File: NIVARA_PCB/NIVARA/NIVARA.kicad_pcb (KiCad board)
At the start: 4 copper layers, 101.2 x 82 mm, 89 parts, among them J1 Power, J10 I_ANALOG, J11 RS485, J12 O_ANALOG, J3 I_NPN, J4 I_PNP, J5 RELAY_1, J6 RELAY_2, J7 O_NPN, J8 O_PNP, J9 I_DIG, Q1 PMBT3904, Q2 PMBT3904, U1 AP63203WU, U10 GP8201S-TC50-EW, U2 AT3H4A-CUH-S, U3 AT3H4A-CUH-S, U4 AT3H4A-CUH-S, U5 AT3H4A-CUH-S, U6 AT3H4A-CUH-S, U7 TD321D485H-A-LB, U8 AT3H4A-CUH-S, U9 GP8303-TC50-EW

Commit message: Se organizaron componentes en el area de PCB
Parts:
- removed C3: C_0603, PCM_Capacitor_SMD_AKL:C_0603_1608Metric
- removed D1: 1N4007, Diode_SMD:D_SOD-123F
- removed L1: L_Iron, Inductor_SMD:L_0201_0603Metric_Pad0.64x0.40mm_HandSolder
- removed Q1: PMBT3904, PCM_Package_TO_SOT_SMD_AKL:SOT-23
- removed R1, R2, R30: 22K, PCM_Resistor_SMD_AKL:R_0603_1608Metric
- removed R23, R31: ?, PCM_Resistor_SMD_AKL:R_0603_1608Metric
- removed R36: ?, PCM_Resistor_SMD_AKL:R_1206_3216Metric_Pad1.30x1.75mm_HandSolder
- removed RLY1: SRD-24VDC-SL-C, easyeda2kicad:RELAY-TH_SRD-XXVDC-XL-C
- removed TP8: TestPoint, TestPoint:TestPoint_THTPad_D1.0mm_Drill0.5mm
- added C16: 220uF, PCM_Capacitor_SMD_AKL:C_0603_1608Metric, F.Cu at (1.18, -49.9)
- added C17: 1uF, PCM_Capacitor_SMD_AKL:C_0603_1608Metric, F.Cu at (1.18, -47.2)
- added C18: 100nF, PCM_Capacitor_SMD_AKL:C_0603_1608Metric, F.Cu at (1.18, -44.5)
- added C19: 1uF, PCM_Capacitor_SMD_AKL:C_0603_1608Metric, F.Cu at (-21.5, -17.4)
- added C20: 100nF, PCM_Capacitor_SMD_AKL:C_0603_1608Metric, F.Cu at (-21.5, -14.6)
- added C21: 1uF, PCM_Capacitor_SMD_AKL:C_0603_1608Metric, F.Cu at (8.18, -23.5)
- added C22: 100nF, PCM_Capacitor_SMD_AKL:C_0603_1608Metric, F.Cu at (8.18, -20.8)
- added C9: 1uF, PCM_Capacitor_SMD_AKL:C_0603_1608Metric, F.Cu at (1.18, -52.6)
- added D4: 1N4007, Diode_SMD:D_SOD-123F, F.Cu at (14.5, -38.6)
- added D5: SM6T24A, Diode_SMD:D_SMB, F.Cu at (17.4, -26.6)
- added D6: SM6T12A, Diode_SMD:D_SMB, F.Cu at (-19.5, -21.5)
- added D7: SM6T12A, Diode_SMD:D_SMB, F.Cu at (3.22, -27.7)
- added JP2: A0, Jumper:SolderJumper-2_P1.3mm_Open_RoundedPad1.0x1.5mm, F.Cu at (1.17, -41.3)
- added JP3: A1, Jumper:SolderJumper-2_P1.3mm_Open_RoundedPad1.0x1.5mm, F.Cu at (1.17, -37.8)
- added JP4: A2, Jumper:SolderJumper-2_P1.3mm_Open_RoundedPad1.0x1.5mm, F.Cu at (1.17, -34.2)
- added L2: FNR5020S3R9NT, easyeda2kicad:IND-SMD_L5.0-W5.0_FNR50XXS, F.Cu at (72.3, 119.9)
- added Q3: BRCS4435SC, easyeda2kicad:SOP-8_L5.0-W4.0-P1.27-LS6.0-BL, F.Cu at (12.9, -49.7)
- added Q4: PMBT3904, PCM_Package_TO_SOT_SMD_AKL:SOT-23, F.Cu at (75.7, -47.4)
- added R10: 1K, PCM_Resistor_SMD_AKL:R_0603_1608Metric, F.Cu at (6.39, -45.5)
- added R11: 2.5K, PCM_Resistor_SMD_AKL:R_0603_1608Metric, F.Cu at (5.41, -36.9)
- added R12: 100K, PCM_Resistor_SMD_AKL:R_0603_1608Metric, F.Cu at (5.41, -34.1)
- added R13: 15R, PCM_Resistor_SMD_AKL:R_1206_3216Metric, F.Cu at (14.6, -42.0)
- added R14: 0R, PCM_Resistor_SMD_AKL:R_0603_1608Metric, F.Cu at (-17.3, -17.4)
- added R15: 0R, PCM_Resistor_SMD_AKL:R_0603_1608Metric, F.Cu at (9.45, -29.1)
- added R16: ?, PCM_Resistor_SMD_AKL:R_0603_1608Metric, F.Cu at (47.1, 87.8)
- added R17: ?, PCM_Resistor_SMD_AKL:R_0603_1608Metric, F.Cu at (48.5, -36.4)
- added R43: 22K, PCM_Resistor_SMD_AKL:R_0603_1608Metric, F.Cu at (71.3, -48.4)
- added R44: ?, PCM_Resistor_SMD_AKL:R_0603_1608Metric, F.Cu at (71.3, -45.7)
- added R7: 150R, PCM_Resistor_SMD_AKL:R_0603_1608Metric, F.Cu at (161.0, 132.4)
- added R8: 1K, PCM_Resistor_SMD_AKL:R_0603_1608Metric, F.Cu at (6.39, -52.3)
- added R9: 1K, PCM_Resistor_SMD_AKL:R_0603_1608Metric, F.Cu at (6.39, -48.9)
- added RLY3: SRD-24VDC-SL-C, easyeda2kicad:RELAY-TH_SRD-XXVDC-XL-C, F.Cu at (125.5, 79.5)
- added TP12: TestPoint, TestPoint:TestPoint_THTPad_D1.0mm_Drill0.5mm, F.Cu at (46.6, 87.8)
- added U11: ESP32-S3-WROOM-1, PCM_Espressif:ESP32-S3-WROOM-1, F.Cu at (153.5, 119.2)
- added U12: ZMM12V_C5345999, easyeda2kicad:LL-34_L3.5-W1.5-RD-2, F.Cu at (14.6, -34.9)
- added U13: GP8201S-TC50-EW, easyeda2kicad:ESOP-8_L4.9-W3.9-P1.27-LS6.0-BL-EP, F.Cu at (2.82, -20.9)
- added kibuzzard-68857B38: G***, kibuzzard-68857B38, F.Cu at (161.0, 134.4)
- added kibuzzard-688671E8: G***, kibuzzard-688671E8, F.Cu at (81.3, 127.7)
- added kibuzzard-688672FE: G***, kibuzzard-688672FE, F.Cu at (81.3, 128.7)
- added kibuzzard-68867375: G***, kibuzzard-68867375, F.Cu at (81.3, 129.7)
- added kibuzzard-68867375: G***, kibuzzard-68867375, F.Cu at (93.9, 129.8)
- added kibuzzard-68867375: G***, kibuzzard-68867375, F.Cu at (87.4, 129.7)
- added kibuzzard-68867375: G***, kibuzzard-68867375, F.Cu at (100.0, 129.7)
- added kibuzzard-688673E6: G***, kibuzzard-688673E6, F.Cu at (87.4, 127.7)
- added kibuzzard-6886740D: G***, kibuzzard-6886740D, F.Cu at (87.4, 128.7)
- added kibuzzard-68868B65: G***, kibuzzard-68868B65, F.Cu at (161.0, 135.9)
- added kibuzzard-68868CAC: G***, kibuzzard-68868CAC, F.Cu at (71.1, 133.0)
- added kibuzzard-68868CE5: G***, kibuzzard-68868CE5, F.Cu at (76.2, 133.0)
- added kibuzzard-68868D86: G***, kibuzzard-68868D86, F.Cu at (83.7, 133.0)
- added kibuzzard-68868DBB: G***, kibuzzard-68868DBB, F.Cu at (88.8, 133.0)
- added kibuzzard-68868E7D: G***, kibuzzard-68868E7D, F.Cu at (96.3, 133.0)
- added kibuzzard-68868E8A: G***, kibuzzard-68868E8A, F.Cu at (101.4, 133.0)
- added kibuzzard-68868F64: G***, kibuzzard-68868F64, F.Cu at (108.6, 133.0)
- added kibuzzard-68868F72: G***, kibuzzard-68868F72, F.Cu at (113.7, 133.0)
- added kibuzzard-68869F01: G***, kibuzzard-68869F01, F.Cu at (87.4, 130.7)
- added kibuzzard-68869F01: G***, kibuzzard-68869F01, F.Cu at (81.3, 130.7)
- added kibuzzard-6886A071: G***, kibuzzard-6886A071, F.Cu at (99.5, 116.1)
- added kibuzzard-6886A071: G***, kibuzzard-6886A071, F.Cu at (93.4, 116.2)
- added kibuzzard-6886A0F4: G***, kibuzzard-6886A0F4, F.Cu at (80.8, 114.6)
- added kibuzzard-6886A148: G***, kibuzzard-6886A148, F.Cu at (86.9, 114.6)
- added kibuzzard-6886AD53: G***, kibuzzard-6886AD53, F.Cu at (86.9, 116.1)
- added kibuzzard-6886AD61: G***, kibuzzard-6886AD61, F.Cu at (80.8, 116.1)
- added kibuzzard-6886ADA1: G***, kibuzzard-6886ADA1, F.Cu at (93.4, 114.7)
- added kibuzzard-6886ADC6: G***, kibuzzard-6886ADC6, F.Cu at (99.5, 114.6)
- added kibuzzard-6886ADE0: G***, kibuzzard-6886ADE0, F.Cu at (93.9, 127.8)
- added kibuzzard-6886ADF2: G***, kibuzzard-6886ADF2, F.Cu at (93.9, 128.8)
- added kibuzzard-6886AE03: G***, kibuzzard-6886AE03, F.Cu at (93.9, 130.9)
- added kibuzzard-6886AE16: G***, kibuzzard-6886AE16, F.Cu at (100.0, 130.7)
- added kibuzzard-6886AE38: G***, kibuzzard-6886AE38, F.Cu at (100.0, 127.7)
- added kibuzzard-6886AE62: G***, kibuzzard-6886AE62, F.Cu at (100.0, 128.7)
- added kibuzzard-6886CB2B: G***, kibuzzard-6886CB2B, F.Cu at (70.4, 116.1)
- added kibuzzard-6886CB54: G***, kibuzzard-6886CB54, F.Cu at (70.4, 114.6)
- C1: footprint PCM_Capacitor_SMD_AKL:C_0603_1608Metric -> PCM_Capacitor_SMD_AKL:C_1206_3216Metric
- C10, C11, C12, C13, C14, C15: value C_0603 -> 1uF
- C4, C5: footprint PCM_Capacitor_SMD_AKL:C_0603_1608Metric -> PCM_Capacitor_SMD_AKL:C_0805_2012Metric
- D3: value SMBJ12CA -> 1N4007; footprint PCM_Diode_SMD_AKL:D_SMB_TVS -> Diode_SMD:D_SOD-123F
- R20, R39, R40: value ? -> 50R
- R21: value 1K -> 10K; footprint PCM_Resistor_SMD_AKL:R_1206_3216Metric_Pad1.30x1.75mm_HandSolder -> PCM_Resistor_SMD_AKL:R_0603_1608Metric
- R22: value 10K -> 50R
- R24, R25, R4, R6: footprint PCM_Resistor_SMD_AKL:R_1206_3216Metric_Pad1.30x1.75mm_HandSolder -> PCM_Resistor_SMD_AKL:R_0603_1608Metric
- R5: value ? -> 1K; footprint PCM_Resistor_SMD_AKL:R_1206_3216Metric_Pad1.30x1.75mm_HandSolder -> PCM_Resistor_SMD_AKL:R_0603_1608Metric
- moved R6 263.4 mm to (157.0, 132.4), turned to 180 degrees
- moved R42 259.4 mm to (153.4, 132.4)
- moved R3 244.8 mm to (138.5, 131.9), turned to 90 degrees
- moved C4 241.1 mm to (76.6, 124.6), turned to -90 degrees
- moved R41 240.7 mm to (138.5, 128.4), turned to 90 degrees
- moved C5 238.6 mm to (74.3, 124.7), turned to -90 degrees
- moved JP1 234.1 mm to (77.6, 120.9)
- moved C2 231.8 mm to (67.3, 119.1)
- moved C1 230.9 mm to (65.2, 126.3), turned to -90 degrees
- moved TP1 226.7 mm to (73.5, 116.3)
- moved U1 226.3 mm to (66.6, 121.9)
- moved R5 224.1 mm to (89.9, 129.7), turned to -90 degrees
- moved TP10 217.2 mm to (102.0, 116.3)
- moved C8 200.0 mm to (161.1, 130.3), turned to 180 degrees
- moved C7 199.9 mm to (157.1, 130.3), turned to 180 degrees
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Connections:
- net /NIVARA_BOARD/ESP32 S3/D_IN1 renamed /NIVARA_BOARD/ESP32 S3/DRY_IN2
- net /NIVARA_BOARD/OUT A 0-10V/SCLK renamed /NIVARA_BOARD/OUT A 0-10V/I2C.SLCK
- net /NIVARA_BOARD/OUT A 0-10V/SDA renamed /NIVARA_BOARD/OUT A 0-10V/I2C.SDA
- net /NIVARA_BOARD/OUT A 4-20mA/SDA renamed /NIVARA_BOARD/ESP32 S3/I2C.SDA
- net /NIVARA_BOARD/OUT A 4-20mA/SLCK renamed /NIVARA_BOARD/ESP32 S3/I2C.SLCK
- net /NIVARA_BOARD/RELAY/EN2 renamed /NIVARA_BOARD/ESP32 S3/RELAY_OUT2
- C15 pad 1: /NIVARA_BOARD/ESP32 S3/D_IN2 -> /NIVARA_BOARD/ESP32 S3/DRY_IN1
- D3 pad 1: unconnected-(D3-K-Pad1) -> VCC
- D3 pad 2: unconnected-(D3-A-Pad2) -> Net-(D3-A)
- J11 pad 1: /NIVARA_BOARD/RS_B -> /NIVARA_BOARD/RS_A
- J11 pad 2: /NIVARA_BOARD/RS_A -> /NIVARA_BOARD/RS_B
- LED10 pad 1: /NIVARA_BOARD/ESP32 S3/D_IN2 -> /NIVARA_BOARD/ESP32 S3/DRY_IN1
- R21 pad 1: Net-(U4-A/C) -> +3V3
- R21 pad 2: /NIVARA_BOARD/NPN_IN2 -> /NIVARA_BOARD/ESP32 S3/NPN_IN2
- R22 pad 2: /NIVARA_BOARD/ESP32 S3/NPN_IN2 -> Net-(LED6-A)
- R38 pad 2: /NIVARA_BOARD/ESP32 S3/D_IN2 -> /NIVARA_BOARD/ESP32 S3/DRY_IN1
- R5 pad 1: Net-(U3-A/C) -> Net-(U4-A/C)
- R5 pad 2: /NIVARA_BOARD/D_IN1 -> /NIVARA_BOARD/NPN_IN2
- TP10 pad 1: /NIVARA_BOARD/ESP32 S3/D_IN2 -> /NIVARA_BOARD/ESP32 S3/PNP_IN2
- U1 pad 1: Net-(U1-FB) -> Net-(JP1-A)
- U10 pad 7: unconnected-(U10-SEL-Pad7) -> Net-(U10-SEL)
- U10 pad 8: unconnected-(U10-V5V-Pad8) -> Net-(U10-V5V)
- U10 pad 9: unconnected-(U10-EP-Pad9) -> GND
- U3 pad 1: Net-(U3-A/C) -> unconnected-(U3-A/C-Pad1)
- U3 pad 2: GND -> Net-(U3-C/A)
- U8 pad 1: Net-(U8-A/C) -> unconnected-(U8-A/C-Pad1)
- U8 pad 2: GND -> Net-(U8-C/A)
- U8 pad 4: /NIVARA_BOARD/ESP32 S3/D_IN2 -> /NIVARA_BOARD/ESP32 S3/DRY_IN1
- U9 pad 10: unconnected-(U9-V5V-Pad10) -> Net-(U9-V5V)
- U9 pad 11: unconnected-(U9-EP-Pad11) -> GND
- U9 pad 6: unconnected-(U9-GND-Pad6) -> GND
- U9 pad 7: unconnected-(U9-SET-Pad7) -> Net-(U9-SET)
- U9 pad 8: /NIVARA_BOARD/A_OUT4_20 -> Net-(U9-IOUT)
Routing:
- net /NIVARA_BOARD/A_IN4_20: track 0.00 -> 20.2 mm
- net Net-(LED7-A): track 0.00 -> 10.6 mm, vias 0 -> 2
- net /NIVARA_BOARD/RS_A: track 0.00 -> 7.91 mm
- net /NIVARA_BOARD/RS_B: track 0.00 -> 6.90 mm
- net GND: track 0.00 -> 4.49 mm, vias 0 -> 53
- net Net-(U1-BST): track 0.00 -> 2.38 mm
- net Net-(U5-A/C): track 0.00 -> 2.15 mm
- net /NIVARA_BOARD/ESP32 S3/PNP_IN1: track 0.00 -> 0.63 mm
- net VCC: vias 0 -> 23
- added copper zone on F.Cu, net +3V3
- added copper zone on F.Cu, net /NIVARA_BOARD/ESP32 S3/PNP_IN1
- added copper zone on F.Cu, net GND
- added copper zone on F.Cu, net Net-(JP1-A)
- added copper zone on F.Cu, net Net-(U1-SW)
- added copper zone on B.Cu, net VCC
- added copper zone on F.Cu, net VCC
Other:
- outline, holes or cut-outs redrawn

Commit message: organizando componentes en la pcb
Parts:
- removed R42: 10K, PCM_Resistor_SMD_AKL:R_0603_1608Metric
- added R18: 2.5K, PCM_Resistor_SMD_AKL:R_0603_1608Metric, F.Cu at (157.5, 132.9)
- added kibuzzard-68867375: G***, kibuzzard-68867375, F.Cu at (106.4, 129.6)
- added kibuzzard-68867375: G***, kibuzzard-68867375, F.Cu at (112.6, 129.6)
- added kibuzzard-688673E6: G***, kibuzzard-688673E6, F.Cu at (112.6, 127.5)
- added kibuzzard-688673E6: G***, kibuzzard-688673E6, F.Cu at (106.4, 127.5)
- added kibuzzard-6886740D: G***, kibuzzard-6886740D, F.Cu at (106.4, 128.5)
- added kibuzzard-6886740D: G***, kibuzzard-6886740D, F.Cu at (112.6, 128.5)
- added kibuzzard-68869F01: G***, kibuzzard-68869F01, F.Cu at (106.4, 130.6)
- added kibuzzard-68869F01: G***, kibuzzard-68869F01, F.Cu at (112.6, 130.6)
- added kibuzzard-6886A148: G***, kibuzzard-6886A148, F.Cu at (105.9, 114.4)
- added kibuzzard-6886A148: G***, kibuzzard-6886A148, F.Cu at (112.1, 114.4)
- added kibuzzard-6886AD53: G***, kibuzzard-6886AD53, F.Cu at (105.9, 115.9)
- added kibuzzard-6886AD53: G***, kibuzzard-6886AD53, F.Cu at (112.1, 115.9)
- added kibuzzard-688D0FD4: G***, kibuzzard-688D0FD4, F.Cu at (138.6, 132.9)
- added kibuzzard-688D1008: G***, kibuzzard-688D1008, F.Cu at (144.2, 132.9)
- added kibuzzard-688D10E8: G***, kibuzzard-688D10E8, F.Cu at (154.1, 132.9)
- added kibuzzard-688D10FC: G***, kibuzzard-688D10FC, F.Cu at (149.7, 132.9)
- R16, R17: value ? -> 1K
- R28, R29, R33, R44: value ? -> 10K
- R6: value 1K -> 22K
- moved U9 237.0 mm to (148.1, 92.4)
- moved C17 204.2 mm to (152.2, 90.4), turned to 90 degrees
- moved R8 203.7 mm to (155.3, 86.7)
- moved JP2 203.1 mm to (158.8, 86.7), turned to 180 degrees
- moved C16 202.5 mm to (150.1, 87.4)
- moved C9 202.4 mm to (144.4, 90.4), turned to 90 degrees
- moved R9 199.3 mm to (155.3, 83.7)
- moved JP3 198.9 mm to (158.8, 83.6), turned to 180 degrees
- moved R10 195.1 mm to (155.3, 80.6)
- moved JP4 195.0 mm to (158.8, 80.6), turned to 180 degrees
- moved C18 194.8 mm to (149.6, 81.7), turned to -90 degrees
- moved R12 194.0 mm to (154.2, 90.4), turned to 90 degrees
- moved R11 189.4 mm to (150.1, 85.3)
- moved U12 188.9 mm to (152.2, 94.7), turned to 90 degrees
- moved Q3 188.6 mm to (145.6, 84.3)
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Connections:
- J12 pad 1: /NIVARA_BOARD/A_OUT0_05 -> GND
- J12 pad 2: /NIVARA_BOARD/A_OUT0_10 -> /NIVARA_BOARD/A_OUT4_20
- J12 pad 3: /NIVARA_BOARD/A_OUT4_20 -> /NIVARA_BOARD/A_OUT0_10
- J12 pad 4: GND -> /NIVARA_BOARD/A_OUT0_05
- J3 pad 1: /NIVARA_BOARD/PNP_IN1 -> /NIVARA_BOARD/NPN_IN1
- J3 pad 2: /NIVARA_BOARD/PNP_IN2 -> /NIVARA_BOARD/NPN_IN2
- J4 pad 1: /NIVARA_BOARD/NPN_IN1 -> /NIVARA_BOARD/PNP_IN1
- J4 pad 2: /NIVARA_BOARD/NPN_IN2 -> /NIVARA_BOARD/PNP_IN2
- R6 pad 1: GND -> /NIVARA_BOARD/A_IN0_32
- U3 pad 1: unconnected-(U3-A/C-Pad1) -> /NIVARA_BOARD/D_IN2
- U8 pad 1: unconnected-(U8-A/C-Pad1) -> /NIVARA_BOARD/D_IN1
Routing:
- net GND: track 4.49 -> 23.5 mm, vias 53 -> 60
- net /NIVARA_BOARD/ESP32 S3/A_IN0_10: track 0.00 -> 16.3 mm, vias 0 -> 2
- net /NIVARA_BOARD/A_IN0_32: track 0.00 -> 13.4 mm
- net /NIVARA_BOARD/D_IN1: track 0.00 -> 12.2 mm
- net /NIVARA_BOARD/D_IN2: track 0.00 -> 11.7 mm
- net +3V3: track 0.00 -> 8.82 mm
- net /NIVARA_BOARD/A_IN0_10: track 0.00 -> 8.59 mm
- net /NIVARA_BOARD/ESP32 S3/A_IN0_32: track 0.00 -> 8.36 mm
- net /NIVARA_BOARD/PNP_IN2: track 0.00 -> 8.18 mm
- net /NIVARA_BOARD/NPN_IN2: track 0.00 -> 8.15 mm
- net /NIVARA_BOARD/NPN_IN1: track 0.00 -> 7.73 mm
- net /NIVARA_BOARD/PNP_IN1: track 0.00 -> 7.62 mm
- net Net-(U8-C/A): track 0.00 -> 2.15 mm
- net Net-(U6-A/C): track 0.00 -> 2.15 mm
- net Net-(U3-C/A): track 0.00 -> 2.15 mm
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- added copper zone on F.Cu, net /NIVARA_BOARD/ESP32 S3/NPN_IN1
- added copper zone on F.Cu, net /NIVARA_BOARD/ESP32 S3/NPN_IN2
- added copper zone on F.Cu, net /NIVARA_BOARD/ESP32 S3/PNP_IN2
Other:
- outline, holes or cut-outs redrawn

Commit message: ACTUALIZACION DE SALIDAS NPN Y PNP
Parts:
- removed the kibuzzard-688673E6 at (106.4, 127.5)
- removed the kibuzzard-6886740D at (106.4, 128.5)
- removed the kibuzzard-68869F01 at (106.4, 130.6)
- removed the kibuzzard-6886AD53 at (105.9, 115.9)
- removed the kibuzzard-6886AD53 at (112.1, 115.9)
- added D8: 1N4007, Diode_SMD:D_SOD-123F, F.Cu at (87.3, 88.2)
- added D9: 1N4007, Diode_SMD:D_SOD-123F, F.Cu at (81.9, 70.9)
- added Q5: NCV8402xST, Package_TO_SOT_SMD:SOT-223, F.Cu at (69.9, 74.6)
- added Q6: NCV8402xST, Package_TO_SOT_SMD:SOT-223, F.Cu at (87.6, 93.3)
- added Q7: NCV8402xST, Package_TO_SOT_SMD:SOT-223, F.Cu at (82.1, 76.0)
- added Q8: NCV8402xST, Package_TO_SOT_SMD:SOT-223, F.Cu at (75.3, 88.9)
- added R23: 1K, PCM_Resistor_SMD_AKL:R_0603_1608Metric, F.Cu at (72.9, 95.6)
- added R30: 22K, PCM_Resistor_SMD_AKL:R_0603_1608Metric, F.Cu at (77.0, 94.8)
- added R31: 1K, PCM_Resistor_SMD_AKL:R_0603_1608Metric, F.Cu at (67.5, 81.2)
- added R36: 22K, PCM_Resistor_SMD_AKL:R_0603_1608Metric, F.Cu at (71.6, 80.4)
- added R42: 1K, PCM_Resistor_SMD_AKL:R_0603_1608Metric, F.Cu at (88.8, 98.8)
- added R45: 22K, PCM_Resistor_SMD_AKL:R_0603_1608Metric, F.Cu at (90.9, 98.8)
- added R46: 1K, PCM_Resistor_SMD_AKL:R_0603_1608Metric, F.Cu at (83.4, 81.6)
- added R47: 22K, PCM_Resistor_SMD_AKL:R_0603_1608Metric, F.Cu at (85.5, 81.6)
- added kibuzzard-688D4BEB: G***, kibuzzard-688D4BEB, F.Cu at (106.4, 127.5)
- added kibuzzard-688D4BF9: G***, kibuzzard-688D4BF9, F.Cu at (106.4, 128.5)
- added kibuzzard-688D4C16: G***, kibuzzard-688D4C16, F.Cu at (106.1, 130.6)
- added kibuzzard-688D4C3C: G***, kibuzzard-688D4C3C, F.Cu at (105.9, 115.9)
- added kibuzzard-688D4C4D: G***, kibuzzard-688D4C4D, F.Cu at (112.1, 115.9)
- moved C17 12.1 mm to (140.0, 90.5), turned to -90 degrees
- moved R12 12.0 mm to (142.2, 90.4), turned to -90 degrees
- moved U12 9.91 mm to (142.3, 93.8), turned to 180 degrees
- moved C21 0.37 mm to (127.4, 83.3)
- moved Q3 0.26 mm to (145.5, 84.0)
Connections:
- U11 pad 15: unconnected-(U11-GPIO3/TOUCH3/ADC1_CH2-Pad15) -> /NIVARA_BOARD/ESP32 S3/RELAY_OUT1
- U11 pad 16: unconnected-(U11-GPIO46-Pad16) -> /NIVARA_BOARD/ESP32 S3/RELAY_OUT2
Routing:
- net VCC: track 0.00 -> 29.1 mm
- net /NIVARA_BOARD/REL_COM2: track 0.00 -> 25.1 mm
- net /NIVARA_BOARD/REL_COM1: track 0.00 -> 25.1 mm
- net /NIVARA_BOARD/OUT A 4-20mA/A1: track 0.00 -> 18.8 mm, vias 0 -> 2
- net Net-(D2-A): track 0.00 -> 18.7 mm
- net /NIVARA_BOARD/OUT A 4-20mA/A2: track 0.00 -> 18.7 mm, vias 0 -> 2
- net /NIVARA_BOARD/OUT A 4-20mA/A0: track 0.00 -> 17.8 mm, vias 0 -> 2
- net Net-(Q3-G): track 0.00 -> 16.6 mm
- net Net-(LED5-A): track 0.00 -> 11.4 mm, vias 0 -> 2
- net /NIVARA_BOARD/REL_NO2: track 0.00 -> 11.3 mm
- net /NIVARA_BOARD/REL_NC2: track 0.00 -> 11.3 mm
- net /NIVARA_BOARD/REL_NC1: track 0.00 -> 11.3 mm
- net /NIVARA_BOARD/REL_NO1: track 0.00 -> 11.3 mm
- net Net-(D3-A): track 0.00 -> 10.7 mm
- net Net-(U9-IOUT): track 0.00 -> 7.39 mm
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
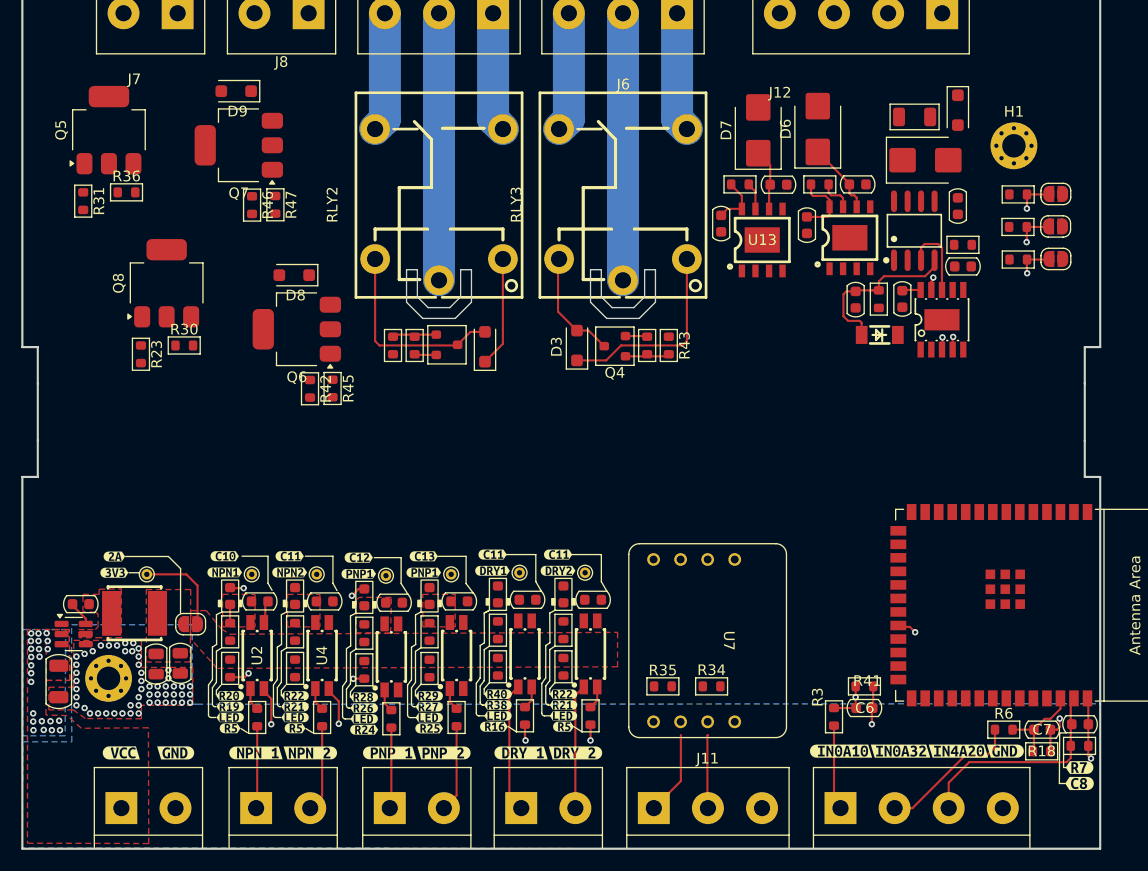
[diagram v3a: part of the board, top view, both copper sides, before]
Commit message: arreglo del desastre que tenia con las salidas PNP
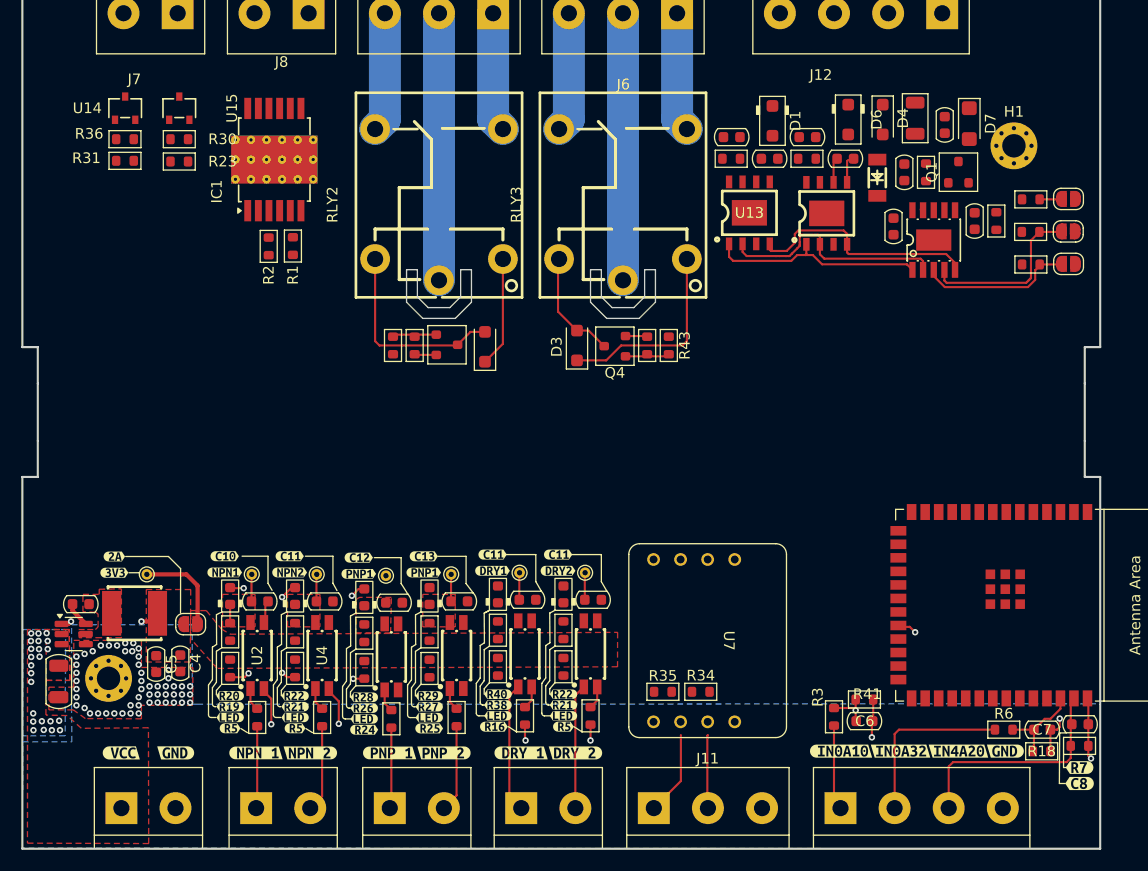
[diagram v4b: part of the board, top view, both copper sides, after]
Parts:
- removed D5: SM6T24A, Diode_SMD:D_SMB
- removed D8, D9: 1N4007, Diode_SMD:D_SOD-123F
- removed Q3: BRCS4435SC, easyeda2kicad:SOP-8_L5.0-W4.0-P1.27-LS6.0-BL
- removed Q5, Q6, Q7, Q8: NCV8402xST, Package_TO_SOT_SMD:SOT-223
- removed R42, R46: 1K, PCM_Resistor_SMD_AKL:R_0603_1608Metric
- removed R45, R47: 22K, PCM_Resistor_SMD_AKL:R_0603_1608Metric
- added D1: SMF11A, PCM_Diode_SMD_AKL:D_SOD-123F, F.Cu at (132.2, 73.7)
- added IC1: ITS5215, Package_SO:Infineon_PG-DSO-12-9_ThermalVias, F.Cu at (85.4, 77.3)
- added Q1: DMP3056L, PCM_Package_TO_SOT_SMD_AKL:SOT-23, F.Cu at (149.7, 78.5)
- added R1: 15K, PCM_Resistor_SMD_AKL:R_0603_1608Metric, F.Cu at (87.2, 85.4)
- added R2: 15K, PCM_Resistor_SMD_AKL:R_0603_1608Metric, F.Cu at (84.9, 85.5)
- added U14: ZXMS6004FFQTA, easyeda2kicad:SOT-23F_L2.9-W1.8-P0.95-LS2.4-BR, F.Cu at (71.4, 72.5)
- added U15: ZXMS6004FFQTA, easyeda2kicad:SOT-23F_L2.9-W1.8-P0.95-LS2.4-BR, F.Cu at (76.5, 72.5)
- C4, C5: footprint PCM_Capacitor_SMD_AKL:C_0805_2012Metric -> PCM_Capacitor_SMD_AKL:C_0603_1608Metric
- D6: value SM6T12A -> SMF11A; footprint Diode_SMD:D_SMB -> PCM_Diode_SMD_AKL:D_SOD-123F
- D7: value SM6T12A -> SMF24A; footprint Diode_SMD:D_SMB -> Diode_SMD:D_SMF
- moved D7 19.8 mm to (150.7, 74.0), turned to -90 degrees
- moved R30 19.4 mm to (76.5, 75.4)
- moved R23 18.5 mm to (76.5, 77.5), turned to 0 degrees
- moved U12 14.8 mm to (142.0, 79.0), turned to 90 degrees
- moved C17 12.8 mm to (144.6, 78.5), turned to 90 degrees
- moved R12 12.7 mm to (146.6, 78.5), turned to 90 degrees
- moved C19 8.27 mm to (135.5, 75.2), turned to 180 degrees
- moved C21 8.18 mm to (128.4, 75.2), turned to 180 degrees
- moved C18 7.72 mm to (148.4, 74.1), turned to 90 degrees
- moved U9 7.52 mm to (147.3, 84.9)
- moved D4 7.11 mm to (142.6, 73.6)
- moved C9 6.86 mm to (143.6, 83.6)
- moved R31 5.45 mm to (71.4, 77.4), turned to 0 degrees
- moved R36 4.99 mm to (71.4, 75.4)
- moved C16 4.41 mm to (151.2, 83.1), turned to -90 degrees
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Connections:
- C18 pad 2: Net-(D5-A1) -> Net-(D7-A1)
- D7 pad 1: /NIVARA_BOARD/A_OUT0_05 -> Net-(D7-A1)
- R13 pad 1: Net-(D5-A1) -> Net-(D7-A1)
- U10 pad 1: /NIVARA_BOARD/OUT A 0-10V/I2C.SLCK -> /NIVARA_BOARD/ESP32 S3/I2C.SLCK
- U10 pad 2: /NIVARA_BOARD/OUT A 0-10V/I2C.SDA -> /NIVARA_BOARD/ESP32 S3/I2C.SDA
- U11 pad 10: /NIVARA_BOARD/ESP32 S3/TX -> unconnected-(U11-GPIO17/U1TXD/ADC2_CH6-Pad10)
- U11 pad 11: /NIVARA_BOARD/ESP32 S3/RX -> unconnected-(U11-GPIO18/U1RXD/ADC2_CH7/CLK_OUT3-Pad11)
- U11 pad 15: /NIVARA_BOARD/ESP32 S3/RELAY_OUT1 -> unconnected-(U11-GPIO3/TOUCH3/ADC1_CH2-Pad15)
- U11 pad 16: /NIVARA_BOARD/ESP32 S3/RELAY_OUT2 -> unconnected-(U11-GPIO46-Pad16)
- U11 pad 25: unconnected-(U11-GPIO48/SPICLK_N/SUBSPICLK_N_DIFF-Pad25) -> /NIVARA_BOARD/ESP32 S3/RX
- U11 pad 26: unconnected-(U11-GPIO45-Pad26) -> /NIVARA_BOARD/ESP32 S3/TX
- U11 pad 4: unconnected-(U11-GPIO4/TOUCH4/ADC1_CH3-Pad4) -> /NIVARA_BOARD/ESP32 S3/I2C.SDA
- U11 pad 5: unconnected-(U11-GPIO5/TOUCH5/ADC1_CH4-Pad5) -> /NIVARA_BOARD/ESP32 S3/I2C.SLCK
- U11 pad 6: unconnected-(U11-GPIO6/TOUCH6/ADC1_CH5-Pad6) -> /NIVARA_BOARD/ESP32 S3/RELAY_OUT1
- U11 pad 7: unconnected-(U11-GPIO7/TOUCH7/ADC1_CH6-Pad7) -> /NIVARA_BOARD/ESP32 S3/RELAY_OUT2
- U13 pad 1: /NIVARA_BOARD/OUT A 0-05V/I2C.SLCK -> /NIVARA_BOARD/ESP32 S3/I2C.SLCK
- U13 pad 2: /NIVARA_BOARD/OUT A 0-05V/I2C.SDA -> /NIVARA_BOARD/ESP32 S3/I2C.SDA
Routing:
- net VCC: track 29.1 -> 51.3 mm
- net /NIVARA_BOARD/ESP32 S3/I2C.SDA: track 0.00 -> 22.2 mm
- net /NIVARA_BOARD/ESP32 S3/I2C.SLCK: track 0.00 -> 20.7 mm
- net Net-(Q1-G): track 16.6 -> 0.00 mm
- net /NIVARA_BOARD/OUT A 4-20mA/A2: track 18.7 -> 2.18 mm, vias 2 -> 0
- net Net-(LED6-A): track 0.00 -> 10.1 mm, vias 0 -> 2
- net Net-(JP1-A): track 0.00 -> 9.41 mm, vias 0 -> 2
- net Net-(Q1-S): track 7.39 -> 0.00 mm
- net Net-(U10-V5V): track 6.47 -> 0.00 mm
- net /NIVARA_BOARD/A_OUT0_05: track 5.75 -> 0.00 mm
- net Net-(U13-V5V): track 4.94 -> 0.00 mm
- net /NIVARA_BOARD/A_OUT0_10: track 6.83 -> 1.93 mm
- net /NIVARA_BOARD/ESP32 S3/DRY_IN2: track 0.00 -> 3.33 mm
- net /NIVARA_BOARD/OUT A 4-20mA/A0: track 17.8 -> 14.5 mm, vias 2 -> 0
- net Net-(U10-SEL): track 3.17 -> 0.00 mm
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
